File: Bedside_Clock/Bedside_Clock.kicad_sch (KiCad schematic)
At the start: 40 parts, among them J1 USBC_USB2.0, SW1 COLOR, SW2 MODE, SW3 BOOT, SW4 RESET, U1 ESP32-C3-MINI-1, U2 USBLC6-2SC6, U3 VEML7700-TT, U4 SN74LVC2T45DCUR

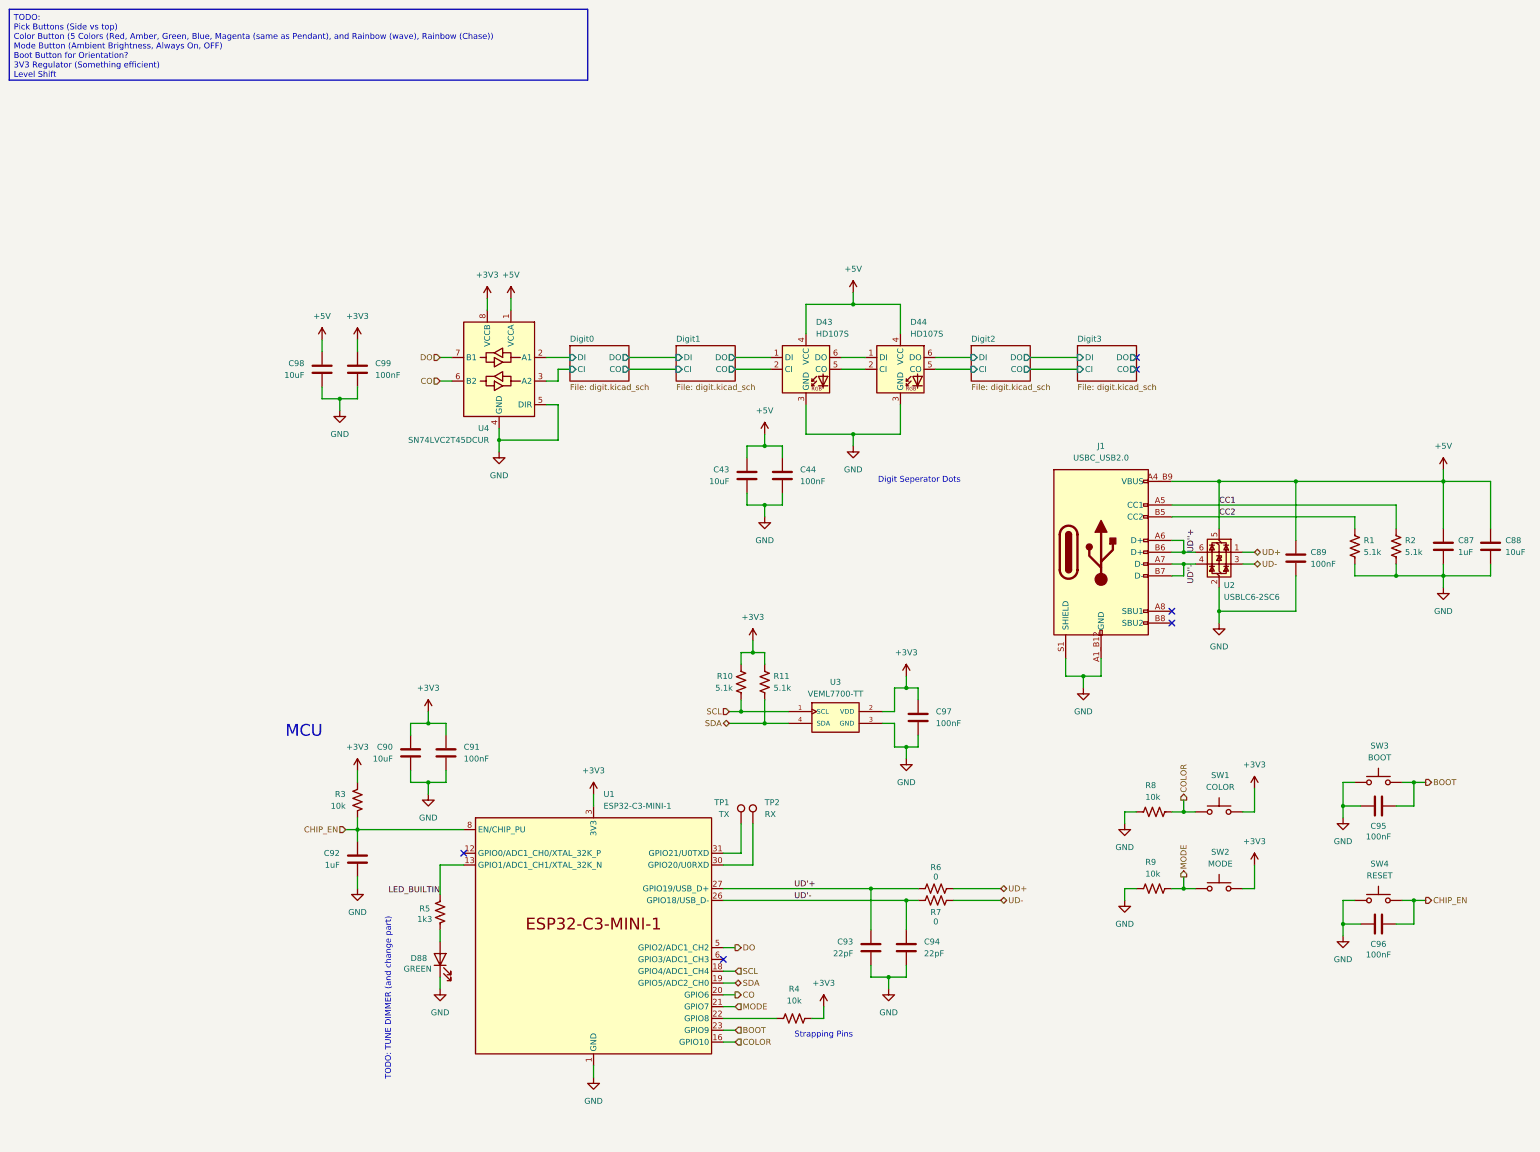
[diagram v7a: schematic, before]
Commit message: [HW] Switch Ambient Light sensor to have proximity
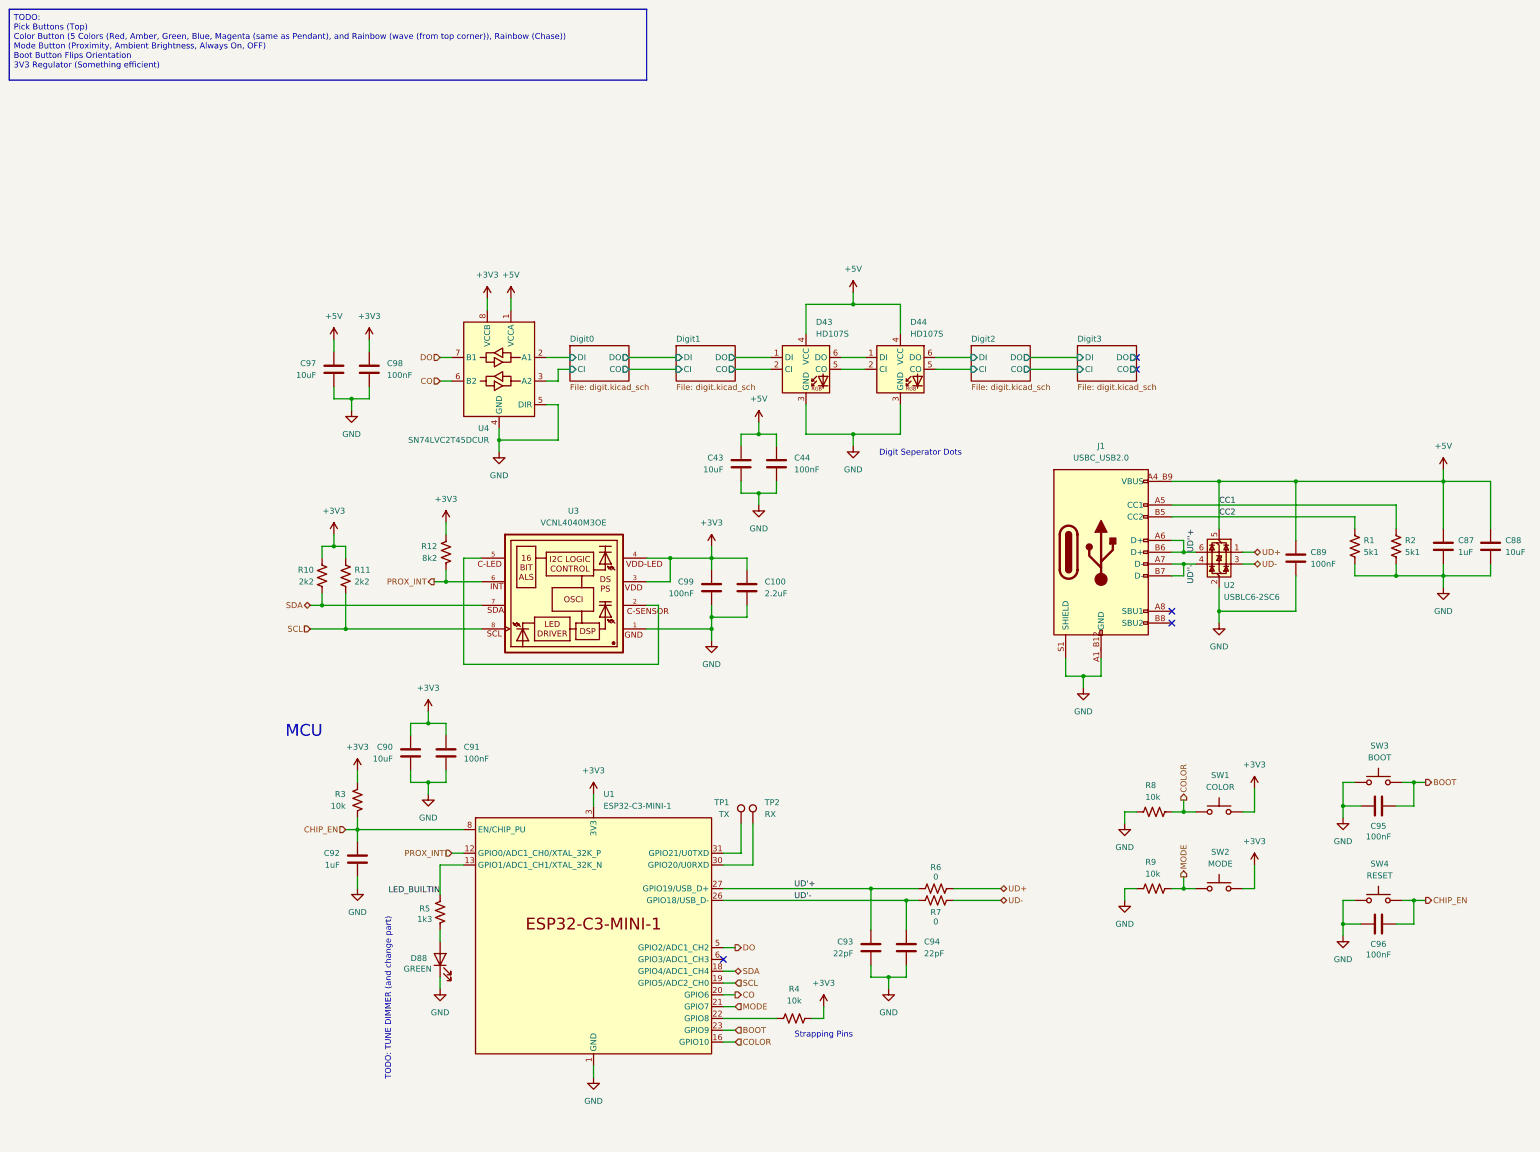
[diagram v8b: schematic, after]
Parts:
- removed C97: 100nF, Capacitor_SMD:C_0603_1608Metric, symbol Device:C
- removed U3: VEML7700-TT, VEML7700_TT:XDCR_VEML7700-TT, symbol VEML7700-TT:VEML7700-TT
- added C100: 2.2uF, Capacitor_SMD:C_0603_1608Metric, symbol Device:C
- added C99: 100nF, Capacitor_SMD:C_0603_1608Metric, symbol Device:C
- added R12: 8k2, Resistor_SMD:R_0603_1608Metric, symbol Device:R_US
- added U3: VCNL4040M3OE, VCNL4040M3OE:VISHAY_VCNL4040_4X2X1.1, symbol VCNL4040M3OE:VCNL4040M3OE
- R1, R2: value 5.1k -> 5k1
- R10, R11: value 5.1k -> 2k2
- U4: footprint SN74LVC2T45DCTR:SOP65P400X130-8N -> Package_SO:VSSOP-8_2.3x2mm_P0.5mm
- renumbered C98 to C97, C99 to C98
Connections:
- net +3V3: now also C100.1, C99.1, R12.2, U3.3, U3.4
- net GND: now also C100.2, C99.2, U3.1
- net SCL: now also R11.1, U1.19 (GPIO5/ADC2_CH0), U3.8; no longer R10.1, U1.18 (GPIO4/ADC1_CH4)
- net SDA: now also R10.1, U1.18 (GPIO4/ADC1_CH4), U3.7; no longer R11.1, U1.19 (GPIO5/ADC2_CH0)
- net PROX_INT: now reaches U1.12 (GPIO0/ADC1_CH0/XTAL_32K_P)
- net PROX_INT: now also R12.1, U3.6
- new net: U3.2, U3.5
- no-connect marks 6 -> 5
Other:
- moved on the sheet: C43, C44, C97, C98, R10, R11
